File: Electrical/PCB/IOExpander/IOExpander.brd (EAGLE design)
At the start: 38 parts, among them U1 MCP23017T-E/SS

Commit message: PCB Batch #1
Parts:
- added A0A1, A2A3, A4A5, A6A7, IA16, IA17, IA18, IA19, IA20, IA21, IA22, IA23, IB16, IB17, IB18, IB19, IB20, IB21, IB22, IB23: JST_1.25_3P, Scott-Connectors:JST1.25_3P
- added F1, F3: (no value), Scott-Electrical:0603
- added H1, H2, H3, H4: HOLE-M3, Scott-Mechanical:M3
- added LA16, LA17, LA18, LA19, LA20, LA21, LA22, LA23, LB16, LB17, LB18, LB19, LB20, LB21, LB22, LB23: JST_1.25_2P, Scott-Connectors:JST1.25_2P
- added MCU2: JST_1.25_6P, Scott-Connectors:JST1.25_6P
- added R1, R17, R19, R21, R23, R24, R3, R5, R7, R8: DNP, Scott-Electrical:0603
- added R18, R2, R20, R22, R4, R6: 10K, Scott-Electrical:0603
- added RA5, RA6, RB5, RB6: (no value), Scott-Electrical:RESCAF80P320X160X60-8N
- added U3: MCP23017T-E/SS, Scott-ICs:SOP65P780X200-28N
- moved LA0 71.5 mm to (48.5, 65.8), turned to 0 degrees
- moved IA0 67.8 mm to (49.8, 59.7), turned to 0 degrees
- moved LA1 64.3 mm to (39.9, 65.8), turned to 0 degrees
- moved IA1 58.9 mm to (39.9, 59.7), turned to 0 degrees
- moved LA2 58.8 mm to (31.2, 65.8), turned to 0 degrees
- moved LA3 55.5 mm to (22.6, 65.8), turned to 0 degrees
- moved IA2 52.2 mm to (30.0, 59.7), turned to 0 degrees
- moved IA3 48.8 mm to (20.1, 59.7), turned to 0 degrees
- moved IA4 48.0 mm to (89.4, 59.7), turned to 0 degrees
- moved LA4 48.0 mm to (88.1, 65.8), turned to 0 degrees
- moved LA5 35.6 mm to (79.5, 65.8), turned to 0 degrees
- moved IA5 34.2 mm to (79.5, 59.7), turned to 0 degrees
- moved IB7 31.7 mm to (24.9, 20.3)
- moved IB4 31.7 mm to (24.9, 50.0)
- moved IB5 31.7 mm to (24.9, 40.1)
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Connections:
- new net ADDR0: R1.1, R2.2, U1.15
- new net ADDR0_2: R17.1, R18.2, U3.15
- new net ADDR1: R3.1, R4.2, U1.16
- new net ADDR1_2: R19.1, R20.2, U3.16
- new net ADDR2: R5.1, R6.2, U1.17
- new net ADDR2_2: R21.1, R22.2, U3.17
- new net C0: IA23.1, LA23.2, RA5.5
- new net C1: IA16.1, LA16.2, RA5.6
- new net C2: IA17.1, LA17.2, RA5.7
- new net C3: IA18.1, LA18.2, RA5.8
- new net C4: IA19.1, LA19.2, RA6.5
- new net C5: IA20.1, LA20.2, RA6.6
- new net C6: IA21.1, LA21.2, RA6.7
- new net C7: IA22.1, LA22.2, RA6.8
- new net D0: IB23.1, LB23.2, RB5.5
- new net D1: IB16.1, LB16.2, RB5.6
- new net D2: IB17.1, LB17.2, RB5.7
- new net D3: IB18.1, LB18.2, RB5.8
- new net D4: IB19.1, LB19.2, RB6.5
- new net D5: IB20.1, LB20.2, RB6.6
- new net D6: IB21.1, LB21.2, RB6.7
- new net D7: IB22.1, LB22.2, RB6.8
- new net INTC: MCU2.2, U3.20
- new net INTD: MCU2.1, U3.19
- new net N$35: RB5.1, U3.4
- new net N$36: RB5.2, U3.3
- new net N$37: RB5.3, U3.2
- new net N$38: RB5.4, U3.1
- new net N$39: RB6.1, U3.8
- new net N$40: RB6.2, U3.7
- new net N$41: RB6.3, U3.6
- new net N$42: RB6.4, U3.5
- new net N$43: RA5.1, U3.24
- new net N$46: RA5.4, U3.21
- new net N$47: RA6.1, U3.28
- new net N$48: RA6.2, U3.27
- new net N$49: RA6.3, U3.26
- new net N$50: RA6.4, U3.25
- new net N$51: F3.2, MCU2.6
- new net N$9: F1.2, MCU.6
- net 3.3V: now also F1.1, F3.1, IA16.3, IA17.3, IA18.3, IA19.3, IA20.3, IA21.3, IA22.3, IA23.3, IB0.3, IB1.3, IB16.3, IB17.3, IB18.3, IB19.3, IB2.3, IB20.3, IB21.3, IB22.3, IB23.3, IB3.3, IB4.3, IB5.3, IB6.3, IB7.3, R1.2, R17.2, R19.2, R21.2, R23.1, R24.1, R3.2, R5.2, R7.1, R8.1, U3.18, U3.9; no longer MCU.6
- net A0: now also A0A1.3
- net A1: now also A0A1.1
- net A2: now also A2A3.3
- net A3: now also A2A3.1
- net A4: now also A4A5.3
- net A5: now also A4A5.1
- net A6: now also A6A7.3
- net A7: now also A6A7.1
- net GND: now also A0A1.2, A2A3.2, A4A5.2, A6A7.2, IA16.2, IA17.2, IA18.2, IA19.2, IA20.2, IA21.2, IA22.2, IA23.2, IB0.2, IB1.2, IB16.2, IB17.2, IB18.2, IB19.2, IB2.2, IB20.2, IB21.2, IB22.2, IB23.2, IB3.2, IB4.2, IB5.2, IB6.2, IB7.2, LA16.1, LA17.1, LA18.1, LA19.1, LA20.1, LA21.1, LA22.1, LA23.1, LB16.1, LB17.1, LB18.1, LB19.1, LB20.1, LB21.1, LB22.1, LB23.1, MCU2.5, R18.1, R2.1, R20.1, R22.1, R4.1, R6.1, U3.10; no longer U1.15, U1.16, U1.17
- net N$44: now also RA5.2, U3.23; no longer IB0.3, IB1.3, IB2.3, IB3.3, IB4.3, IB5.3, IB6.3, IB7.3
- net N$45: now also RA5.3, U3.22; no longer IB0.2, IB1.2, IB2.2, IB3.2, IB4.2, IB5.2, IB6.2, IB7.2
- net SCL: now also MCU2.3, R23.2, R7.2, U3.12
- net SDA: now also MCU2.4, R24.2, R8.2, U3.13
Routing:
- net 3.3V: track 7.98 -> 516.6 mm, vias 2 -> 42
- net SDA: track 10.2 -> 83.3 mm, vias 0 -> 2
- net SCL: track 11.6 -> 83.9 mm
- net A4: track 0.00 -> 61.3 mm
- net A3: track 0.00 -> 60.1 mm, vias 0 -> 2
- net D3: track 0.00 -> 56.3 mm, vias 0 -> 2
- net B3: track 0.00 -> 56.3 mm, vias 0 -> 2
- net A2: track 0.00 -> 52.9 mm, vias 0 -> 2
- net C4: track 0.00 -> 52.1 mm
- net C3: track 0.00 -> 51.5 mm, vias 0 -> 2
- net A5: track 0.00 -> 51.0 mm
- net B2: track 0.00 -> 46.6 mm, vias 0 -> 2
- net D2: track 0.00 -> 46.6 mm, vias 0 -> 2
- net A1: track 0.00 -> 45.0 mm, vias 0 -> 2
- net C2: track 0.00 -> 43.8 mm, vias 0 -> 2
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- added copper zone on layer 1, net 3.3V
- added copper zone on layer 16, net 3.3V
- added copper zone on layer 1, net GND
- added copper zone on layer 16, net GND
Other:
- board outline added: 111.8 x 78.7 mm
- board text added: "0"
- board text added: "1"
- board text added: "2"
- board text added: "A0"
- board text added: "A1"
- board text added: "A2"
- board text added: "A3"
- board text added: "A4"
- board text added: "A5"
- board text added: "A6"
- board text added: "A7"
- board text added: "Addr"
- board text added: "B0"
- board text added: "B1"
- board text added: "B2"
- board text added: "B3"
- board text added: "B4"
- board text added: "B5"
- board text added: "B6"
- board text added: "B7"
- board text added: "C0"
- board text added: "C1"
- board text added: "C2"
- board text added: "C3"
- board text added: "C4"
- board text added: "C5"
- board text added: "C6"
- board text added: "C7"
- board text added: "D0"
- board text added: "D1"
- board text added: "D2"
- board text added: "D3"
- board text added: "D4"
- board text added: "D5"
- board text added: "D6"
- board text added: "D7"
- board text added: "IOExpander V1 Jan 16, 2020"

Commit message: bump pcb 2/24
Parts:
- removed LB0, LB1, LB2, LB3, LB4, LB5, LB6, LB7: JST_1.25_2P, Scott-Connectors:JST1.25_2P
- removed MCU: JST_1.25_6P, Scott-Connectors:JST1.25_6P
- added J0, J1, J2, J3, J4, J5, J6, J7: DNP, Scott-Electrical:0603
- added MCU1: JST_1.25_7P, Scott-Connectors:JST1.25_7P
- added UD0, UD1, UD2, UD3, UD4, UD5, UD6, UD7: DEBOUNCE_MAX6816EUS+T, Scott-ICs:21-0052F
- MCU2: value JST_1.25_6P -> JST_1.25_7P; device Scott-Connectors:JST1.25_6P -> Scott-Connectors:JST1.25_7P
- moved MCU2 1.30 mm to (66.3, 39.4)
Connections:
- removed net N$51: F3.2, MCU2.6
- new net B0D: J3.2, RB1.5, UD0.3
- new net B1D: J2.2, RB1.6, UD1.3
- new net B2D: J1.2, RB1.7, UD2.3
- new net B3D: J0.2, RB1.8, UD3.3
- new net B4D: J7.2, RB2.5, UD4.3
- new net B5D: J6.2, RB2.6, UD5.3
- new net B6D: J5.2, RB2.7, UD6.3
- new net B7D: J4.2, RB2.8, UD7.3
- new net N$18: F3.2, MCU2.7
- new net RST1: MCU1.1, U1.18
- new net RST2: MCU2.1, U3.18
- net 3.3V: now also UD0.4, UD1.4, UD2.4, UD3.4, UD4.4, UD5.4, UD6.4, UD7.4; no longer U1.18, U3.18
- net B0: now also IB3.1, J3.1, UD0.2; no longer IB0.1, LB0.2, RB1.5
- net B1: now also IB2.1, J2.1, UD1.2; no longer IB1.1, LB1.2, RB1.6
- net B2: now also IB1.1, J1.1, UD2.2; no longer IB2.1, LB2.2, RB1.7
- net B3: now also IB0.1, J0.1, UD3.2; no longer IB3.1, LB3.2, RB1.8
- net B4: now also IB7.1, J7.1, UD4.2; no longer IB4.1, LB4.2, RB2.5
- net B5: now also IB6.1, J6.1, UD5.2; no longer IB5.1, LB5.2, RB2.6
- net B6: now also IB5.1, J5.1, UD6.2; no longer IB6.1, LB6.2, RB2.7
- net B7: now also IB4.1, J4.1, UD7.2; no longer IB7.1, LB7.2, RB2.8
- net GND: now also MCU1.6, MCU2.6, UD0.1, UD1.1, UD2.1, UD3.1, UD4.1, UD5.1, UD6.1, UD7.1; no longer LB0.1, LB1.1, LB2.1, LB3.1, LB4.1, LB5.1, LB6.1, LB7.1, MCU.5, MCU2.5
- net INTA: now also MCU1.3; no longer MCU.2
- net INTB: now also MCU1.2; no longer MCU.1
- net INTC: now also MCU2.3; no longer MCU2.2
- net INTD: now also MCU2.2; no longer MCU2.1
- net N$9: now also MCU1.7; no longer MCU.6
- net SCL: now also MCU1.4, MCU2.4; no longer MCU.3, MCU2.3
- net SDA: now also MCU1.5, MCU2.5; no longer MCU.4, MCU2.4
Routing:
- net B0D: track 0.00 -> 66.5 mm, vias 0 -> 2
- net B1D: track 0.00 -> 55.5 mm, vias 0 -> 2
- net B4D: track 0.00 -> 54.4 mm, vias 0 -> 4
- net 3.3V: track 516.6 -> 571.0 mm
- net B3: track 56.3 -> 5.67 mm, vias 2 -> 1
- net B2D: track 0.00 -> 44.5 mm, vias 0 -> 2
- net B5D: track 0.00 -> 43.3 mm, vias 0 -> 3
- net B2: track 46.6 -> 5.40 mm, vias 2 -> 1
- net B3D: track 0.00 -> 33.3 mm, vias 0 -> 2
- net B7: track 38.6 -> 5.66 mm, vias 0 -> 1
- net B1: track 38.0 -> 5.66 mm, vias 2 -> 1
- net B6D: track 0.00 -> 32.2 mm, vias 0 -> 2
- net B0: track 32.5 -> 5.66 mm, vias 2 -> 1
- net B6: track 28.7 -> 5.66 mm, vias 0 -> 1
- net B7D: track 0.00 -> 21.1 mm, vias 0 -> 2
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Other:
- outline, holes or cut-outs redrawn
- board text added: "Debounced Ch.B"
- board text added: "IOExpander V2.1 Feb 24, 2020"
- board text added: "MultiFunction Ch.A"
- board text added: "MultiFunction Ch.C"
- board text added: "MultiFunction Ch.D"
- board text added: "Short to disable debounce"
- board text removed: "IOExpander V1 Jan 16, 2020"

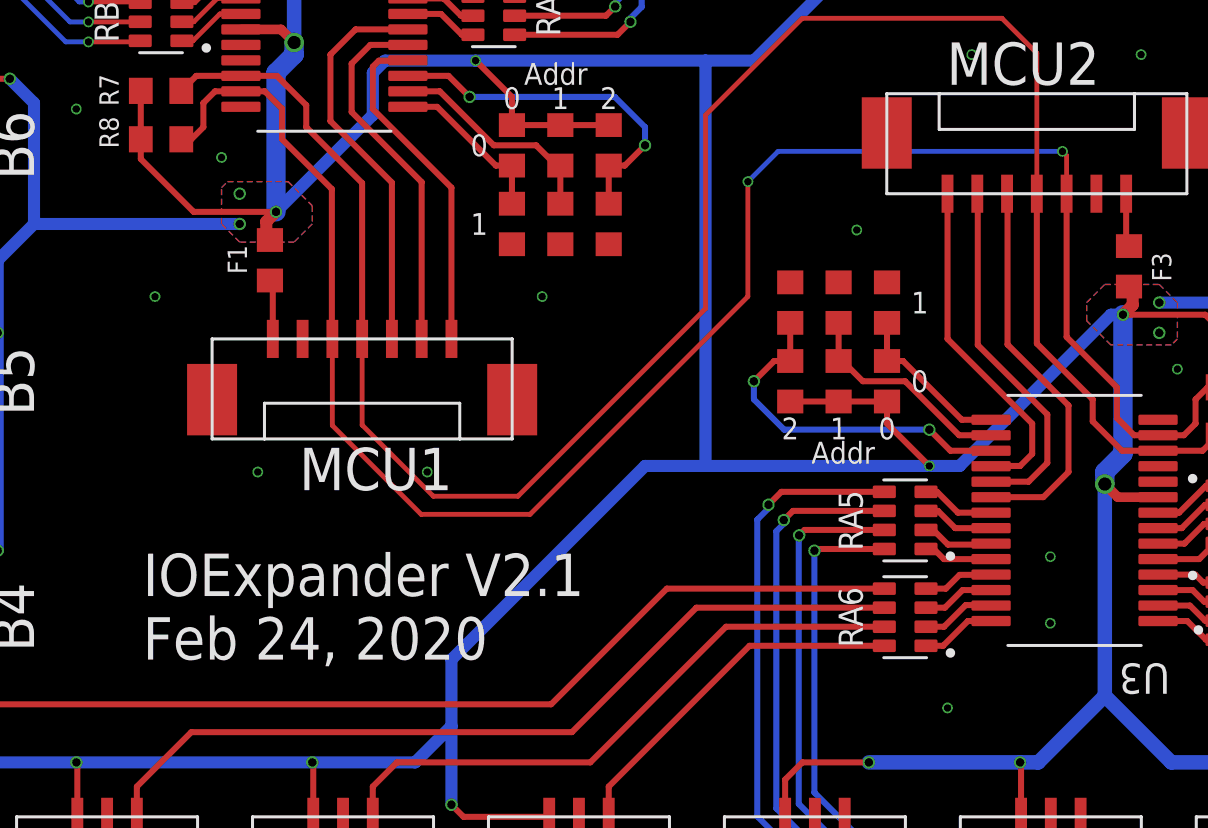
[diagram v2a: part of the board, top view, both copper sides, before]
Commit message: io expander fix V2.2 -- add 0.1uF to GND on IRQ pin
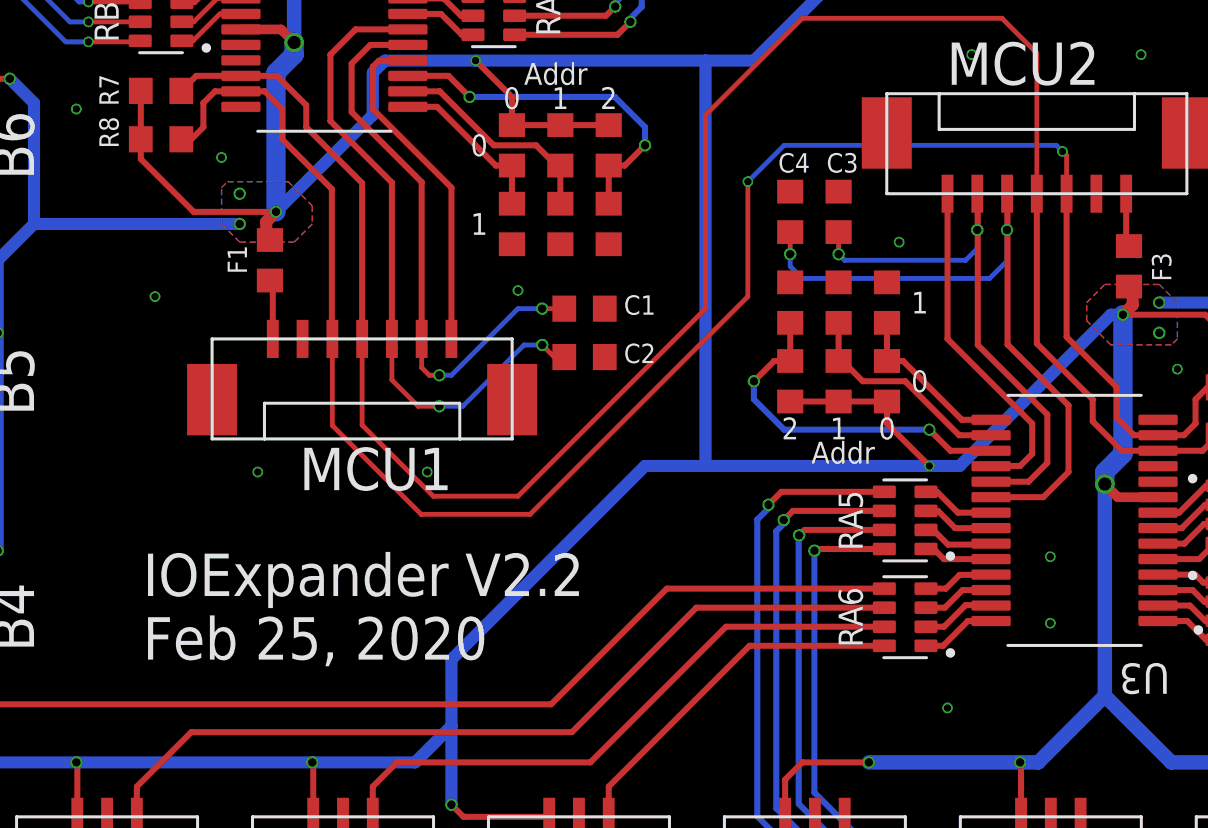
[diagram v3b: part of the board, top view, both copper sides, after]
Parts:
- added C1, C2, C3, C4: 0.1uF, Scott-Electrical:0603
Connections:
- net GND: now also C1.2, C2.2, C3.2, C4.2
- net INTA: now also C2.1
- net INTB: now also C1.1
- net INTC: now also C4.1
- net INTD: now also C3.1
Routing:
- net INTC: track 16.4 -> 30.3 mm, vias 0 -> 2
- net INTA: track 16.7 -> 27.4 mm, vias 0 -> 2
- net INTD: track 15.2 -> 24.6 mm, vias 0 -> 2
- net INTB: track 15.5 -> 23.9 mm, vias 0 -> 2
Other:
- board text added: "IOExpander V2.2 Feb 25, 2020"
- board text removed: "IOExpander V2.1 Feb 24, 2020"
